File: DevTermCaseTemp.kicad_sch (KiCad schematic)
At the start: 1 part, among them J1 miniPCIe

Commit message: in production. good luck!
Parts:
- added C1, C4, C5: 10uF, Capacitor_SMD:C_0805_2012Metric, symbol Device:C
- added C10, C2, C9: 1uF, Capacitor_SMD:C_0805_2012Metric, symbol Device:C
- added C11, C14, C15, C16, C17, C3, C6, C7, C8: 100nF, Capacitor_SMD:C_0805_2012Metric, symbol Device:C
- added C12, C13: 20pF, Capacitor_SMD:C_0805_2012Metric, symbol Device:C
- added D1, D10, D11, D12, D13, D14, D15, D16, D17, D18, D19, D2, D3, D4, D5, D6, D9: ESD, Diode_SMD:D_SOD-323, symbol Diode:ESD9B5.0ST5G
- added D7, D8: LED, LED_SMD:LED_0603_1608Metric, symbol Device:LED
- added FB1, FB2: FerriteBead, Capacitor_SMD:C_0805_2012Metric, symbol Device:FerriteBead_Small
- added H1, H2, H3: MountingHole_Pad, MountingHole:MountingHole_2.7mm_M2.5_DIN965_Pad, symbol Mechanical:MountingHole_Pad
- added J1, J3: USB_A, Connector_USB:USB_A_CONNFLY_DS1095-WNR0, symbol Connector:USB_A
- added J4: USB_B_Micro, Connector_USB:USB_Micro-B_Amphenol_10118194_Horizontal, symbol Connector:USB_B_Micro
- added J5: JBAT, Connector_PinSocket_2.00mm:PinSocket_1x02_P2.00mm_Horizontal, symbol Connector_Generic:Conn_01x02
- added J6: Conn_01x04, Connector_PinSocket_2.00mm:PinSocket_1x04_P2.00mm_Horizontal, symbol Connector_Generic:Conn_01x04
- added J7, J8: DevTermSpeaker, devterm-ext-outline:DevTerm-Speaker, symbol devterm_speaker:DevTermSpeaker
- added J9: Conn_02x22_Odd_Even, devterm-ext-outline:C64_expansion_2x22_socket, symbol Connector_Generic:Conn_02x22_Odd_Even
- added JP1: A2, Connector_PinHeader_2.54mm:PinHeader_1x03_P2.54mm_Horizontal, symbol Jumper:SolderJumper_3_Open
- added JP2: A1, Connector_PinHeader_2.54mm:PinHeader_1x03_P2.54mm_Horizontal, symbol Jumper:SolderJumper_3_Open
- added JP3: A0, Connector_PinHeader_2.54mm:PinHeader_1x03_P2.54mm_Horizontal, symbol Jumper:SolderJumper_3_Open
- added R1, R9: 30K, Resistor_SMD:R_0805_2012Metric, symbol Device:R
- added R10, R4, R5: 10K, Resistor_SMD:R_0805_2012Metric, symbol Device:R
- added R11, R7: 6.8K/1%, Resistor_SMD:R_0805_2012Metric, symbol Device:R
- added R12, R14, R17, R18: 1K, Resistor_SMD:R_0805_2012Metric, symbol Device:R
- added R13: 15K, Resistor_SMD:R_0805_2012Metric, symbol Device:R
- added R15, R16, R19, R3, R6: 100K, Resistor_SMD:R_0805_2012Metric, symbol Device:R
- added R2: 680R/1%, Resistor_SMD:R_0805_2012Metric, symbol Device:R
- added R8: 47K, Resistor_SMD:R_0805_2012Metric, symbol Device:R
- added SW1: SW_DIP_x02, Button_Switch_SMD:SW_DIP_SPSTx02_Slide_6.7x6.64mm_W6.73mm_P2.54mm_LowProfile_JPin, symbol Switch:SW_DIP_x02
- added U1: GL850G, GL850G:SSOP28, symbol GL850G:GL850G
- added U10, U11, U7, U8: 4052, Package_SO:SOIC-16_3.9x9.9mm_P1.27mm, symbol 4xxx:4052
- added U12: TXS0102DCU, Package_SO:VSSOP-8_2.3x2mm_P0.5mm, symbol Logic_LevelTranslator:TXS0102DCU
- added U2, U3: SY6280, SY6280:SOT23-5P95_285X100L45X40N, symbol sy6280:SY6280
- added U4: DS1307+, devterm-ext-outline:SOIC-8, symbol Timer_RTC:DS1307+
- added U5: MCP23008-xSS, Package_SO:SOIC-20W_7.5x12.8mm_P1.27mm, symbol Interface_Expansion:MCP23008-xSS
- added U6: CH340N, Package_SO:SOP-8_3.9x4.9mm_P1.27mm, symbol wch-usb-uart:CH340N
- added U9: gp7101, Package_SO:SOP-8_3.9x4.9mm_P1.27mm, symbol gp7101:gp7101
- added Y1: 12MHz, Crystal:Crystal_SMD_3225-4Pin_3.2x2.5mm_HandSoldering, symbol Device:Crystal_GND24
- added Y2: 32.768KHz, Crystal:Crystal_DS26_D2.0mm_L6.0mm_Horizontal, symbol Device:Crystal
- J2: renamed from J1; value miniPCIe -> EXT_miniPCIe
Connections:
- net +3.3V: now also C16.1, C3.1, C5.1, FB1.2, FB2.1, JP1.3 (B), JP2.3 (B), JP3.3 (B), R13.1, R6.2, U1.24, U12.3 (VCCA), U12.6 (OE), U3.5 (IN), U5.20 (VDD)
- net +5V: now also C17.1, J6.1 (Pin_1), R3.2, R4.1, SW1.1, SW1.2, U1.23, U10.16 (VDD), U11.16 (VDD), U12.7 (VCCB), U2.5 (IN), U4.8 (VCC), U7.16 (VDD), U8.16 (VDD), U9.8 (VCC)
- net GND: now also C1.2, C10.2, C11.2, C12.2, C13.2, C14.2, C15.1, C16.2, C17.2, C2.2, C3.2, C4.2, C5.2, C6.2, C7.2, C8.2, C9.2, D1.2 (A2), D10.1 (A1), D11.1 (A1), D12.1 (A1), D13.1 (A1), D14.1 (A1), D15.1 (A1), D16.1 (A1), D17.1 (A1), D18.1 (A1), D19.1 (A1), D2.1 (A1), D3.1 (A1), D4.2 (A2), D5.1 (A1), D6.1 (A1), D9.1 (A1), H1.1, H2.1, H3.1, J1.4 (GND), J1.5 (Shield), J3.4 (GND), J3.5 (Shield), J4.4 (ID), J4.5 (GND), J4.6 (Shield), J5.2 (Pin_2), J6.2 (Pin_2), J6.4 (Pin_4), J9.22 (Pin_22), J9.23 (Pin_23), JP1.1 (A), JP2.1 (A), JP3.1 (A), R11.2, R15.2, R16.2, R2.1, R7.2, R8.2, R9.2, U1.15, U10.7 (VEE), U10.8 (VSS), U11.7 (VEE), U11.8 (VSS), U12.2 (GND), U2.2 (GND), U3.2 (GND), U4.4 (GND), U5.9 (VSS), U6.3 (GND), U7.7 (VEE), U7.8 (VSS), U8.7 (VEE), U8.8 (VSS), U9.5 (GND), U9.6 (PWM), Y1.2, Y1.4
- net IO28: now also J9.13 (Pin_13)
- net IO29: now also J9.15 (Pin_15)
- net IO30: now also J9.17 (Pin_17)
- net IO31: now also J9.19 (Pin_19)
- net IO32: now also U7.4 (Y3), U8.12 (X0), U8.14 (X1), U8.15 (X2)
- net IO33: now also U7.11 (X3), U8.1 (Y0), U8.2 (Y2), U8.5 (Y1)
- net IO34: now also J9.14 (Pin_14)
- net IO35: now also J9.16 (Pin_16)
- net IO36: now also R10.1, R5.1
- net IO37: now also U10.2 (Y2), U10.5 (Y1), U11.12 (X0), U8.11 (X3)
- net IO38: now also J9.18 (Pin_18)
- net IO39: now also J9.20 (Pin_20)
- net IO40: now also U10.12 (X0), U11.14 (X1), U11.15 (X2), U8.4 (Y3)
- net IO41: now also U10.1 (Y0), U10.11 (X3), U10.14 (X1), U10.15 (X2)
- net IO42: now also U10.4 (Y3), U11.1 (Y0), U11.2 (Y2), U11.5 (Y1)
- net IO43: now also J9.21 (Pin_21), R19.2, U10.6 (Inh), U11.6 (Inh), U7.6 (Inh), U8.6 (Inh)
- net IO44: now also U11.11 (X3), U7.12 (X0), U7.14 (X1), U7.15 (X2)
- net IO45: now also U11.4 (Y3), U7.1 (Y0), U7.2 (Y2), U7.5 (Y1)
- net SPK_LN: now also J7.2 (N1), J7.4 (N2)
- net SPK_LP: now also J7.1 (P1), J7.3 (P2)
- net SPK_RN: now also J8.2 (N1), J8.4 (N2)
- net SPK_RP: now also J8.1 (P1), J8.3 (P2)
- net CAM_C_N renamed CAM.C-
- net CAM.C-: now also J9.8 (Pin_8)
- net CAM_C_P renamed CAM.C+
- net CAM.C+: now also J9.7 (Pin_7)
- net CAM_D0_N renamed CAM0.D-
- net CAM0.D-: now also J9.12 (Pin_12)
- net CAM_D0_P renamed CAM0.D+
- net CAM0.D+: now also J9.11 (Pin_11)
- net CAM_D1_N renamed CAM1.D-
- net CAM1.D-: now also J9.10 (Pin_10)
- net CAM_D1_P renamed CAM1.D+
- net CAM1.D+: now also J9.9 (Pin_9)
- net CAM_D2_N renamed CAM2.D-
- net CAM_D2_P renamed CAM2.D+
- net CAM_D3_N renamed CAM3.D-
- net CAM_D3_P renamed CAM3.D+
- net USB3_D_N renamed USB3.D-
- net USB3.D-: now also D6.2 (A2), J3.2 (D-)
- net USB3_D_P renamed USB3.D+
- net USB3.D+: now also D5.2 (A2), J3.3 (D+)
- net USB4_D_N renamed USB4.D-
- net USB4.D-: now also U1.25
- net USB4_D_P renamed USB4.D+
- net USB4.D+: now also U1.26
- new net: R18.1, U6.7 (RXD)
- new net: D10.2 (A2), J4.3 (D+), U6.1 (UD+)
- new net: D11.2 (A2), J4.2 (D-), U6.2 (UD-)
- new net: R17.1, U6.6 (TXD)
- new net: C14.1, U6.8 (V3)
- new net: FB1.1, U1.16
- new net: R2.2, U1.4
- new net: R1.2, R9.1, U1.19, U1.21
- new net: R3.1, U1.17
- new net: D8.2 (A), R14.2
- new net: C15.2, R13.2, U5.6 (~{RESET})
- new net: J5.1 (Pin_1), U4.3 (VBAT)
- new net: U12.4 (A2), U7.13 (X)
- new net: U12.5 (A1), U7.3 (Y)
- new net: D7.2 (A), R12.2
- new net: JP3.2 (C), U5.5 (A0)
- new net: JP2.2 (C), U5.4 (A1)
- new net: R6.1, U1.18
- new net: C2.1, R4.2, R8.1, U1.13
- new net: U4.1 (X1), Y2.1
- new net: U4.2 (X2), Y2.2
- new net: JP1.2 (C), U5.3 (A2)
- new net: R7.1, U2.3 (ISET)
- new net: R5.2, U2.4 (EN)
- new net: R11.1, U3.3 (ISET)
- new net: R10.2, U3.4 (EN)
- new net +3.3VP: C4.1, D13.2 (A2), J9.2 (Pin_2), J9.43 (Pin_43), R19.1, U3.1 (OUT)
- new net +5VP: C1.1, D1.1 (A1), D12.2 (A2), D4.1 (A1), J1.1 (VBUS), J3.1 (VBUS), J9.1 (Pin_1), J9.44 (Pin_44), R1.1, U2.1 (OUT)
- new net AVDD: C10.1, C11.1, C6.1, C7.1, C8.1, C9.1, FB2.2, U1.1, U1.10, U1.5
- new net EXT_GPIO0: J9.39 (Pin_39), U5.12 (GP0)
- new net EXT_GPIO1: J9.37 (Pin_37), U5.13 (GP1)
- new net EXT_GPIO2: J9.35 (Pin_35), U5.14 (GP2)
- new net EXT_GPIO3: J9.33 (Pin_33), U5.15 (GP3)
- new net EXT_GPIO4: J9.31 (Pin_31), U5.16 (GP4)
- new net EXT_GPIO5: J9.29 (Pin_29), U5.17 (GP5)
- new net EXT_GPIO6: J9.27 (Pin_27), U5.18 (GP6)
- new net EXT_GPIO7: J9.25 (Pin_25), U5.19 (GP7)
- new net EXT_USB1.D+: D14.2 (A2), J9.3 (Pin_3), U1.28
- new net EXT_USB1.D-: D15.2 (A2), J9.4 (Pin_4), U1.27
- new net EXT_USB2.D+: D16.2 (A2), J9.42 (Pin_42), U1.3
- new net EXT_USB2.D-: D17.2 (A2), J9.41 (Pin_41), U1.2
- new net EXT_USB3.D+: D18.2 (A2), J9.5 (Pin_5), U1.9
- new net EXT_USB3.D-: D19.2 (A2), J9.6 (Pin_6), U1.8
- new net EXT_USB4.D+: D2.2 (A2), J1.3 (D+), U1.12
- new net EXT_USB4.D-: D3.2 (A2), J1.2 (D-), U1.11
- new net EXT_USB_X1: C12.1, U1.6, Y1.1
- new net EXT_USB_X2: C13.1, U1.7, Y1.3
- new net GPIO_X1: J9.38 (Pin_38), U11.13 (X)
- new net GPIO_X2: J9.40 (Pin_40), U11.3 (Y)
- new net I2C_SCL: J9.32 (Pin_32), U12.8 (B1), U4.6 (SCL), U5.1 (SCL), U9.2 (SDA)
- new net I2C_SDA: J9.30 (Pin_30), U12.1 (B2), U4.5 (SDA), U5.2 (SDA), U9.1 (SCLK)
- new net ID_A: R15.1, SW1.4, U10.10 (A), U11.10 (A), U7.10 (A), U8.10 (A)
- new net ID_B: R16.1, SW1.3, U10.9 (B), U11.9 (B), U7.9 (B), U8.9 (B)
- new net SPI_CS: J9.26 (Pin_26), U10.13 (X)
- new net SPI_MISO: J9.28 (Pin_28), U10.3 (Y)
- new net UART_RX: D8.1 (K), J9.34 (Pin_34), R17.2, U8.3 (Y)
- new net UART_TX: D7.1 (K), J9.36 (Pin_36), R18.2, U8.13 (X)
- new net VBUS: D9.2 (A2), J4.1 (VBUS), R12.1, R14.1, U6.5 (VCC)
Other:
- note added: "ADDR=0x58 BAUD=100K"
- note added: "ADDR=0xD0"
- note added: "CARTRIDGE"
- note added: "Commandore64-style expansion port. Pin assignment desiderata: - Maximum compatibility and function alignment. - Strong coupling of differential pairs. - Avoid damage. All power pins are mirror safe. Expansion port requirement: - Pin 21 MUST connect to Pin 23. - Pin 24 MUST be NC ROUTE_EN disconnects all routed pins when cartridge is: - Disconnected - Inserted the wrong direction Resource overview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"
- note added: "DEBUG"
- note added: "DEVTERM EXT BOARD"
- note added: "DIP 0 0 =A06 IO32-UART_TX IO33-UART_RX IO37-GPIO_X1 IO40-SPI_CS IO41-SPI_MISO IO42-GPIO_X2 IO44-I2C_SDA IO45-I2C_SCL"
- note added: "DIP 0 1 =CM3 IO32-UART_TX IO33-UART_RX IO37-SPI_MISO IO40-GPIO_X1 IO41-SPI_CS [SOFT] IO42-GPIO_X2 IO44-I2C_SDA IO45-I2C_SCL"
- note added: "DIP 1 0 =CM4(?) IO32-UART_TX IO33-UART_RX IO37-SPI_MISO IO40-GPIO_X1 IO41-SPI_CS IO42-GPIO_X2 IO44-I2C_SDA IO45-I2C_SCL"
- note added: "DIP 1 1 =R01 IO32-I2C_SCL IO33-I2C_SDA IO37-UART_TX IO40-UART_RX IO41-SPI_CS IO42-SPI_MISO IO44-GPIO_X1 IO45-GPIO_X2"
- note added: "GPIO-EXP"
- note added: "MiniPCIE"
- note added: "POWER"
- note added: "PWMFAN"
- note added: "R"
- note added: "R=Reserved"
- note added: "RTC"
- note added: "Routing"
- note added: "SPEAKER"
- note added: "USB"

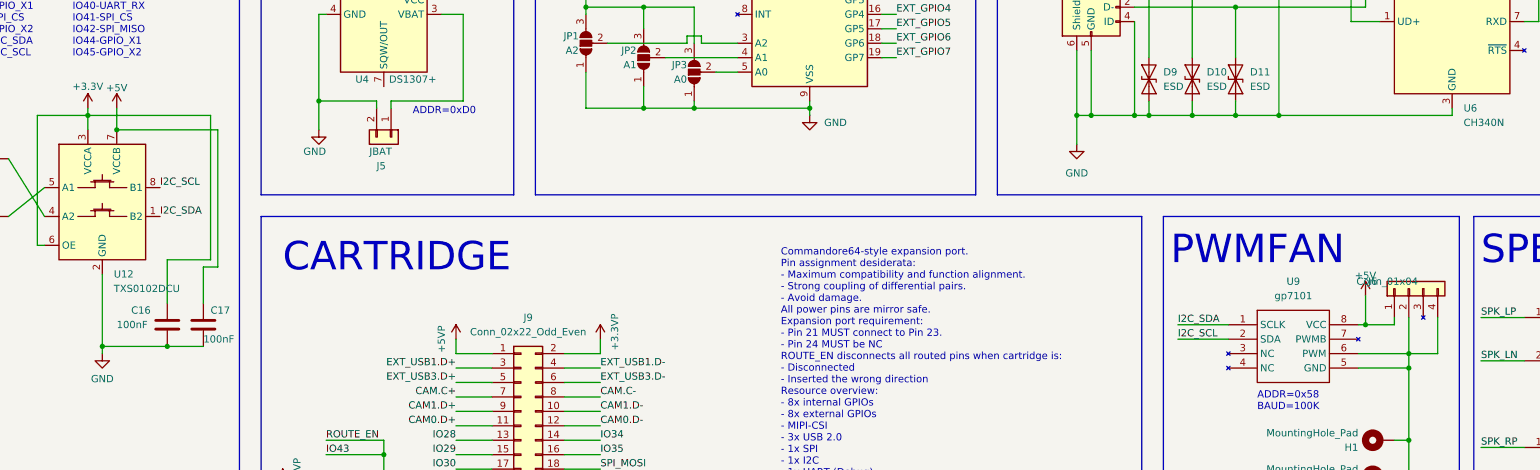
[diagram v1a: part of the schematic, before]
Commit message: i2c level shifter to ssop
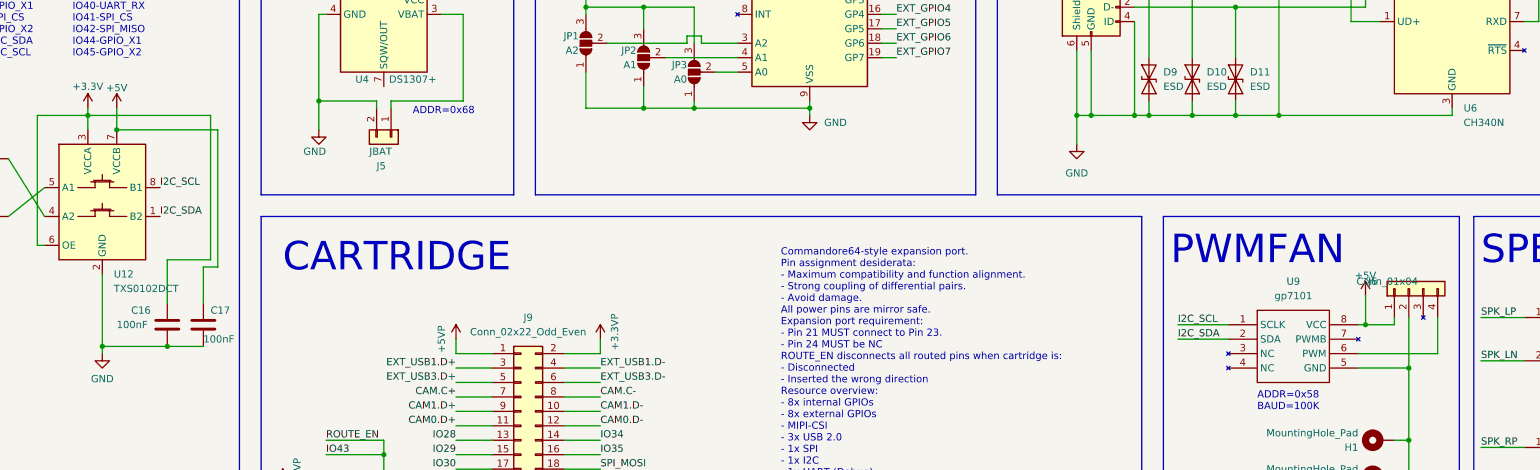
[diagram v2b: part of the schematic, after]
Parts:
- removed U12: TXS0102DCU, Package_SO:VSSOP-8_2.3x2mm_P0.5mm, symbol Logic_LevelTranslator:TXS0102DCU
- added U12: TXS0102DCT, Package_SO:SSOP-8_2.95x2.8mm_P0.65mm, symbol Logic_LevelTranslator:TXS0102DCT
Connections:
- net +3.3V: now also U12.3 (VCCA), U12.6 (OE)
- net +5V: now also U12.7 (VCCB)
- net GND: now also U12.2 (GND); no longer J6.4 (Pin_4), U9.6 (PWM)
- net I2C_SCL: now also U9.1 (SCLK), U12.8 (B1); no longer U9.2 (SDA)
- net I2C_SDA: now also U9.2 (SDA), U12.1 (B2); no longer U9.1 (SCLK)
- net at U7.13 (X): now also U12.4 (A2)
- net at U7.3 (Y): now also U12.5 (A1)
- new net: J6.4 (Pin_4), U9.6 (PWM)
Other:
- note added: "ADDR=0x68"
- note removed: "ADDR=0xD0"
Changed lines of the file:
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@@
   (junction (at 55.88 78.74) (diameter 0) (color 0 0 0 0)
   )
-  (junction (at 115.57 170.18) (diameter 0) (color 0 0 0 0)
-  )
   (junction (at 339.09 85.09) (diameter 0) (color 0 0 0 0)
   )
@@
   (junction (at 83.82 213.36) (diameter 0) (color 0 0 0 0)
   )
-  (junction (at 342.9 209.55) (diameter 0) (color 0 0 0 0)
-  )
   (junction (at 208.28 148.59) (diameter 0) (color 0 0 0 0)
   )
@@
   (junction (at 245.11 44.45) (diameter 0) (color 0 0 0 0)
   )
+  (junction (at 115.57 170.18) (diameter 0) (color 0 0 0 0)
+  )
   (junction (at 353.06 127) (diameter 0) (color 0 0 0 0)
   )
@@
     (stroke (width 0) (type default) (color 0 0 0 0))
   )
-  (wire (pts (xy 342.9 209.55) (xy 347.98 209.55))
+  (wire (pts (xy 334.01 209.55) (xy 347.98 209.55))
     (stroke (width 0) (type default) (color 0 0 0 0))
   )
@@
     (stroke (width 0) (type default) (color 0 0 0 0))
   )
-  (wire (pts (xy 342.9 212.09) (xy 342.9 209.55))
+  (wire (pts (xy 342.9 203.2) (xy 342.9 212.09))
     (stroke (width 0) (type default) (color 0 0 0 0))
   )
@@
     (stroke (width 0) (type default) (color 0 0 0 0))
   )
-  (wire (pts (xy 334.01 209.55) (xy 342.9 209.55))
-    (stroke (width 0) (type default) (color 0 0 0 0))
-  )
   (wire (pts (xy 40.64 45.72) (xy 40.64 50.8))
     (stroke (width 0) (type default) (color 0 0 0 0))
@@
     (stroke (width 0) (type default) (color 0 0 0 0))
   )
+  (wire (pts (xy 113.03 195.58) (xy 113.03 208.28))
+    (stroke (width 0) (type default) (color 0 0 0 0))
+  )
   (wire (pts (xy 55.88 71.12) (xy 55.88 78.74))
     (stroke (width 0) (type default) (color 0 0 0 0))
@@
     (stroke (width 0) (type default) (color 0 0 0 0))
   )
-  (wire (pts (xy 342.9 203.2) (xy 342.9 209.55))
-    (stroke (width 0) (type default) (color 0 0 0 0))
-  )
   (wire (pts (xy 386.08 80.01) (xy 386.08 85.09))
     (stroke (width 0) (type default) (color 0 0 0 0))
@@
     (stroke (width 0) (type default) (color 0 0 0 0))
   )
-  (wire (pts (xy 113.03 208.28) (xy 113.03 195.58))
-    (stroke (width 0) (type default) (color 0 0 0 0))
-  )
   (wire (pts (xy 57.15 40.64) (xy 55.88 40.64))
     (stroke (width 0) (type default) (color 0 0 0 0))
@@
     (effects (font (size 5 5)) (justify left bottom))
   )
-  (text "ADDR=0xD0" (at 167.64 167.64 0)
+  (text "ADDR=0x68" (at 167.64 167.64 0)
     (effects (font (size 1.27 1.27)) (justify left bottom))
   )
@@
     (effects (font (size 1.27 1.27)) (justify right bottom))
   )
-  (label "I2C_SCL" (at 302.26 207.01 0)
+  (label "I2C_SDA" (at 302.26 207.01 0)
     (effects (font (size 1.27 1.27)) (justify left bottom))
   )
@@
     (effects (font (size 1.27 1.27)) (justify left bottom))
   )
-  (label "I2C_SDA" (at 302.26 204.47 0)
+  (label "I2C_SCL" (at 302.26 204.47 0)
     (effects (font (size 1.27 1.27)) (justify left bottom))
   )
@@
     (pin "2")
   )
-  (symbol (lib_id "Logic_LevelTranslator:TXS0102DCU") (at 113.03 182.88 0) (unit 1)
-    (in_bom yes) (on_board yes) (fields_autoplaced)
-    (property "Reference" "U12" (id 0) (at 115.0494 195.58 0)
-      (effects (font (size 1.27 1.27)) (justify left))
-    )
-    (property "Value" "TXS0102DCU" (id 1) (at 115.0494 198.12 0)
-      (effects (font (size 1.27 1.27)) (justify left))
-    )
-    (property "Footprint" "Package_SO:VSSOP-8_2.3x2mm_P0.5mm" (id 2) (at 113.03 196.85 0)
-      (effects (font (size 1.27 1.27)) hide)
-    )
-    (property "Datasheet" "http://www.ti.com/lit/gpn/txs0102" (id 3) (at 113.03 183.388 0)
-      (effects (font (size 1.27 1.27)) hide)
-    )
-    (pin "1")
-    (pin "2")
-    (pin "3")
-    (pin "4")
-    (pin "5")
-    (pin "6")
-    (pin "7")
-    (pin "8")
-  )
   (symbol (lib_id "Device:C") (at 323.85 134.62 270) (unit 1)
     (in_bom yes) (on_board yes) (fields_autoplaced)
@@
     (pin "1")
   )
+  (symbol (lib_id "Logic_LevelTranslator:TXS0102DCT") (at 113.03 182.88 0) (unit 1)
+    (in_bom yes) (on_board yes) (fields_autoplaced)
+    (property "Reference" "U12" (id 0) (at 115.0494 195.58 0)
+      (effects (font (size 1.27 1.27)) (justify left))
+    )
+    (property "Value" "TXS0102DCT" (id 1) (at 115.0494 198.12 0)
+      (effects (font (size 1.27 1.27)) (justify left))
+    )
+    (property "Footprint" "Package_SO:SSOP-8_2.95x2.8mm_P0.65mm" (id 2) (at 113.03 196.85 0)
+      (effects (font (size 1.27 1.27)) hide)
+    )
+    (property "Datasheet" "http://www.ti.com/lit/gpn/txs0102" (id 3) (at 113.03 183.388 0)
+      (effects (font (size 1.27 1.27)) hide)
+    )
+    (pin "1")
+    (pin "2")
+    (pin "3")
+    (pin "4")
+    (pin "5")
+    (pin "6")
+    (pin "7")
+    (pin "8")
+  )
   (symbol (lib_id "Device:R") (at 269.24 48.26 0) (unit 1)
     (in_bom yes) (on_board yes) (fields_autoplaced)
@@
       (reference "U11") (unit 1) (value "4052") (footprint "Package_SO:SOIC-16_3.9x9.9mm_P1.27mm")
     )
-    (path "/55664dcb-dff5-4d77-a2dc-c7081cbed3f7"
-      (reference "U12") (unit 1) (value "TXS0102DCU") (footprint "Package_SO:VSSOP-8_2.3x2mm_P0.5mm")
+    (path "/9a1c98c5-ba5b-4762-ad44-0d4c206c43a4"
+      (reference "U12") (unit 1) (value "TXS0102DCT") (footprint "Package_SO:SSOP-8_2.95x2.8mm_P0.65mm")
     )
     (path "/b5e5ee02-fa80-4e4d-99e7-5707c4fe2a87"

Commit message: v3 is finalized
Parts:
- J1, J3: footprint Connector_USB:USB_A_CONNFLY_DS1095-WNR0 -> devterm-ext-outline:USB_A_PCBCUT
- J6: footprint Connector_PinSocket_2.00mm:PinSocket_1x04_P2.00mm_Horizontal -> Connector_PinSocket_2.00mm:PinSocket_1x04_P2.00mm_Vertical
- J9: footprint devterm-ext-outline:C64_expansion_2x22_socket -> devterm-ext-outline:C64-Cart-Socket-Horizontal
- JP1: value A2 -> A0; footprint Connector_PinHeader_2.54mm:PinHeader_1x03_P2.54mm_Horizontal -> Jumper:SolderJumper-3_P1.3mm_Open_Pad1.0x1.5mm
- JP2: footprint Connector_PinHeader_2.54mm:PinHeader_1x03_P2.54mm_Horizontal -> Jumper:SolderJumper-3_P1.3mm_Open_Pad1.0x1.5mm
- JP3: value A0 -> A2; footprint Connector_PinHeader_2.54mm:PinHeader_1x03_P2.54mm_Horizontal -> Jumper:SolderJumper-3_P1.3mm_Open_Pad1.0x1.5mm
- SW1: footprint Button_Switch_SMD:SW_DIP_SPSTx02_Slide_6.7x6.64mm_W6.73mm_P2.54mm_LowProfile_JPin -> Button_Switch_SMD:SW_DIP_SPSTx02_Slide_6.7x6.64mm_W8.61mm_P2.54mm_LowProfile
- U12: footprint Package_SO:SSOP-8_2.95x2.8mm_P0.65mm -> Package_SO:MSOP-8_3x3mm_P0.65mm
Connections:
- net GND: now also U7.6 (Inh)
- net GPIO_X1: now also J9.30 (Pin_30); no longer J9.38 (Pin_38)
- net GPIO_X2: now also J9.32 (Pin_32); no longer J9.40 (Pin_40)
- net I2C_SCL: now also J9.19 (Pin_19); no longer J9.32 (Pin_32)
- net I2C_SDA: now also J9.17 (Pin_17); no longer J9.30 (Pin_30)
- net IO28: now also J9.34 (Pin_34); no longer J9.13 (Pin_13)
- net IO29: now also J9.36 (Pin_36); no longer J9.15 (Pin_15)
- net IO30: now also J9.38 (Pin_38); no longer J9.17 (Pin_17)
- net IO31: now also J9.40 (Pin_40); no longer J9.19 (Pin_19)
- net IO43: no longer U7.6 (Inh), U8.6 (Inh)
- net UART_RX: now also J9.13 (Pin_13); no longer J9.34 (Pin_34)
- net UART_TX: now also J9.15 (Pin_15); no longer J9.36 (Pin_36)
- net at U5.5 (A0): now also JP1.2 (C); no longer JP3.2 (C)
- net at U5.3 (A2): now also JP3.2 (C); no longer JP1.2 (C)
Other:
- note added: "No cart=Hi-Z"

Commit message: File cleanup
Moved library files into /lib/ directory, moved media in /media/ folder
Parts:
- removed H1, H2, H3: MountingHole_Pad, MountingHole:MountingHole_2.7mm_M2.5_DIN965_Pad, symbol Mechanical:MountingHole_Pad
- added R20: 10K, Resistor_SMD:R_0805_2012Metric, symbol Device:R
- added SW2: SW_SPDT, Button_Switch_THT:SW_CuK_OS102011MA1QN1_SPDT_Angled, symbol Switch:SW_SPDT
- added U13: DevTermFan3505, devterm-ext-outline:turbo_fan_3505, symbol devterm_symbols:DevTermFan3505
- J5: value JBAT -> Conn_01x02; footprint Connector_PinSocket_2.00mm:PinSocket_1x02_P2.00mm_Horizontal -> Connector_Molex:Molex_PicoBlade_53048-0210_1x02_P1.25mm_Horizontal
- J7, J8: symbol devterm_speaker:DevTermSpeaker -> devterm_symbols:DevTermSpeaker
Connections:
- net GND: now also U8.6 (Inh), R20.1, U13.1 (GND); no longer J9.23 (Pin_23)
- net UART_RX: now also SW2.1 (A); no longer D8.1 (K), R17.2, U8.3 (Y)
- net UART_TX renamed DBG_TX
- new net: SW2.2 (B), U8.3 (Y)
- new net: J9.23 (Pin_23), R20.2
- new net DBG_RX: D8.1 (K), R17.2, SW2.3 (C)
- no-connect marks 0 -> 1
